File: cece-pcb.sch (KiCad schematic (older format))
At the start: 29 parts, among them J101 VAC, J102 HTU21D, J103 SERIAL, J104 Li-Ion Battery, K101 SANYOU_SRD_Form_C, Q101 Q_NPN, U101 TLV75533PDBV, U102 MCP73811T-420I-OT

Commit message: Improve ACDC converter design to make it more robust
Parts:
- removed C103: 1u, Capacitor_THT:C_Radial_D6.3mm_H5.0mm_P2.50mm, symbol Device:C
- removed J104: Li-Ion Battery, Connector_PinHeader_2.54mm:PinHeader_1x02_P2.54mm_Vertical, symbol Connector_Generic:Conn_01x02
- removed JP102: VBATT 5V, Jumper:SolderJumper-2_P1.3mm_Open_Pad1.0x1.5mm, symbol Jumper:SolderJumper_2_Open
- removed JP103: 73811, Jumper:SolderJumper-2_P1.3mm_Open_Pad1.0x1.5mm, symbol Jumper:SolderJumper_2_Open
- removed R105: R_PROG, Resistor_SMD:R_0805_2012Metric_Pad1.15x1.40mm_HandSolder, symbol Device:R_US
- removed U102: MCP73811T-420I-OT, Package_TO_SOT_SMD:SOT-23-5, symbol Battery_Management:MCP73811T-420I-OT
- added C101: 100u, Capacitor_THT:CP_Radial_D6.3mm_P2.50mm, symbol Device:CP
- added D101: SMBJ5.0A, Diode_SMD:D_SMB_Handsoldering, symbol Device:D_Zener
- added F101: 1A slow blow, Capacitor_THT:C_Disc_D8.0mm_W5.0mm_P5.00mm, symbol Device:Fuse
- added RV101: 10D561K, Capacitor_THT:C_Disc_D7.5mm_W5.0mm_P7.50mm, symbol Device:Varistor
- added VP101: VimarPlana, pol:vimar_plana_3P, symbol pol:VimarPlana
- C102: footprint Capacitor_THT:C_Radial_D6.3mm_H5.0mm_P2.50mm -> Capacitor_SMD:C_0805_2012Metric_Pad1.15x1.40mm_HandSolder
- renumbered C101 to C103, D101 to D102, D102 to D103, D103 to D105, D105 to D106, R103 to R102, R104 to R103
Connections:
- wire segments 100 -> 101
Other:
- note added: "ACDC converter schematic from:\nhttps://datasheet.lcsc.com/szlcsc/1811211452_GTL-POWER-VB02-T2S03_C335526.pdf\nWith values from:\nhttp://www.hlktech.net/product_detail.php?ProId=54"
- moved on the sheet: D104, D106, J103, PS101, U101

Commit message: Separate top and bottom PCBs
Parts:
- removed C101: 100u, Capacitor_THT:CP_Radial_D6.3mm_P2.50mm, symbol Device:CP
- removed C103: 10u, Capacitor_THT:C_Radial_D6.3mm_H5.0mm_P2.50mm, symbol Device:CP
- removed D101: SMBJ5.0A, Diode_SMD:D_SMB_Handsoldering, symbol Device:D_Zener
- removed D102: 1N4001, Diode_THT:D_DO-41_SOD81_P7.62mm_Horizontal, symbol Diode:1N4001
- removed D103, D105: LED, LED_THT:LED_D3.0mm, symbol Device:LED
- removed F101: 1A slow blow, Capacitor_THT:C_Disc_D8.0mm_W5.0mm_P5.00mm, symbol Device:Fuse
- removed H101, H102, H103, H104: MountingHole_Pad, MountingHole:MountingHole_3.2mm_M3_Pad, symbol Mechanical:MountingHole_Pad
- removed J101: VAC, TerminalBlock:TerminalBlock_bornier-5_P5.08mm, symbol Connector:Screw_Terminal_01x05
- removed JP101: VBATT_A0, Jumper:SolderJumper-2_P1.3mm_Bridged_Pad1.0x1.5mm, symbol Jumper:SolderJumper_2_Bridged
- removed K101: SANYOU_SRD_Form_C, Relay_THT:Relay_SPDT_SANYOU_SRD_Series_Form_C, symbol Relay:SANYOU_SRD_Form_C
- removed PS101: HLK-PM01, Converter_ACDC:Converter_ACDC_HiLink_HLK-PMxx, symbol Converter_ACDC:HLK-PM01
- removed Q101: Q_NPN, Package_TO_SOT_THT:TO-92L_Inline_Wide, symbol Device:Q_NPN_CBE
- removed RV101: 10D561K, Capacitor_THT:C_Disc_D7.5mm_W5.0mm_P7.50mm, symbol Device:Varistor
- added C101, C103: 1u, Capacitor_SMD:C_0805_2012Metric_Pad1.15x1.40mm_HandSolder, symbol Device:C
- added C104: 100nF, Capacitor_THT:C_Disc_D4.3mm_W1.9mm_P5.00mm, symbol Device:C
- added C105, C106: 100p, Capacitor_SMD:C_0805_2012Metric_Pad1.15x1.40mm_HandSolder, symbol Device:C
- added FB101: Ferrite_Bead, Resistor_SMD:R_0805_2012Metric_Pad1.15x1.40mm_HandSolder, symbol Device:Ferrite_Bead
- added JP101: RST, Connector_PinHeader_2.54mm:PinHeader_1x02_P2.54mm_Vertical, symbol Device:Jumper_NO_Small
- added JP102: PROG, Connector_PinHeader_2.54mm:PinHeader_1x02_P2.54mm_Vertical, symbol Device:Jumper_NO_Small
- added JP103: Deep_Sleep, Jumper:SolderJumper-2_P1.3mm_Open_Pad1.0x1.5mm, symbol Jumper:SolderJumper_2_Open
- added R104: 10k, Resistor_SMD:R_0805_2012Metric_Pad1.15x1.40mm_HandSolder, symbol Device:R_US
- added R105, R107: 330, Resistor_SMD:R_0805_2012Metric_Pad1.15x1.40mm_HandSolder, symbol Device:R_US
- added R106: 10k, Resistor_THT:R_Axial_DIN0207_L6.3mm_D2.5mm_P7.62mm_Horizontal, symbol Device:R_US
- added U102: ESP-12F/ESP07, RF_Module:ESP-07, symbol cece-pcb-rescue:ESP-12F-ESP8266-cece-pcb-rescue
- added U103: LM75C, symbol Sensor_Temperature:LM75C
- C102: value 1u -> 10u
- R101: value 220 -> 10k; footprint Resistor_THT:R_Axial_DIN0207_L6.3mm_D2.5mm_P7.62mm_Horizontal -> Resistor_SMD:R_0805_2012Metric_Pad1.15x1.40mm_HandSolder
- R102: value 1k -> 10k; footprint Resistor_THT:R_Axial_DIN0207_L6.3mm_D2.5mm_P7.62mm_Horizontal -> Resistor_SMD:R_0805_2012Metric_Pad1.15x1.40mm_HandSolder
- R103: value 100 -> 10k; footprint Resistor_THT:R_Axial_DIN0207_L6.3mm_D2.5mm_P7.62mm_Horizontal -> Resistor_SMD:R_0805_2012Metric_Pad1.15x1.40mm_HandSolder
- renumbered D104 to D101, D106 to D102, J103 to J101
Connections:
- net labels added: ADC, D0, D1|SCL, D2|SDA, D3, D4, D5|SCK, D6|MISO, D7|MOSI, D8, EN, RST
- net labels removed: +BATT, ACL, ACN, C, HTU_SCL, HTU_SDA, NC, NO, RLY
- wire segments 101 -> 99
- no-connect marks 0 -> 10
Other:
- note added: "Basic input protection from:\nhttps://www.digikey.com/en/articles/protecting-inputs-in-digital-electronics"
- note added: "https://escapequotes.net/wp-content/uploads/2016/02/wemos-d1-mini-shematics.jpg"
- note added: "https://www.wemos.cc/en/latest/_static/files/sch_d1_mini_v3.0.0.pdf"
- note removed: "ACDC converter schematic from:\nhttps://datasheet.lcsc.com/szlcsc/1811211452_GTL-POWER-VB02-T2S03_C335526.pdf\nWith values from:\nhttp://www.hlktech.net/product_detail.php?ProId=54"
- moved on the sheet: D101, D102, J101, J102

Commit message: Start defining PCB
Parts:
- added C107, C108: 100nF, Capacitor_SMD:C_0805_2012Metric_Pad1.15x1.40mm_HandSolder, symbol Device:C
- added J103: Conn_01x03_Male, Connector_PinSocket_2.54mm:PinSocket_1x03_P2.54mm_Vertical, symbol Connector:Conn_01x03_Male
- added SW101, SW102: SW_Push, Button_Switch_THT:SW_PUSH_6mm, symbol Switch:SW_Push
- C104: footprint Capacitor_THT:C_Disc_D4.3mm_W1.9mm_P5.00mm -> Capacitor_SMD:C_0805_2012Metric_Pad1.15x1.40mm_HandSolder
- R106: footprint Resistor_THT:R_Axial_DIN0207_L6.3mm_D2.5mm_P7.62mm_Horizontal -> Resistor_SMD:R_0805_2012Metric_Pad1.15x1.40mm_HandSolder
- U103: footprint (none) -> Package_SO:SOIC-8_3.9x4.9mm_P1.27mm
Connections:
- net +5V: now also J103.3 (Pin_3)
- net D4: now also SW102.1
- net D5|SCK: now also SW101.1
- net D8: now also J103.2 (Pin_2)
- net GND: now also J103.1 (Pin_1), SW101.2, SW102.2
- no-connect marks 10 -> 9
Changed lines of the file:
@@
 F 0 "U103" H 10200 6381 50  0000 C CNN
 F 1 "LM75C" H 10200 6290 50  0000 C CNN
-F 2 "" H 10200 5700 50  0001 C CNN
+F 2 "Package_SO:SOIC-8_3.9x4.9mm_P1.27mm" H 10200 5700 50  0001 C CNN
 F 3 "http://www.ti.com/lit/ds/symlink/lm75b.pdf" H 10200 5700 50  0001 C CNN
 	1    10200 5700
@@
 F 0 "C104" H 5815 3796 50  0000 L CNN
 F 1 "100nF" H 5815 3705 50  0000 L CNN
-F 2 "Capacitor_THT:C_Disc_D4.3mm_W1.9mm_P5.00mm" H 5738 3600 50  0001 C CNN
+F 2 "Capacitor_SMD:C_0805_2012Metric_Pad1.15x1.40mm_HandSolder" H 5738 3600 50  0001 C CNN
 F 3 "~" H 5700 3750 50  0001 C CNN
 	1    5700 3750
@@
 F 0 "R106" H 8232 3604 50  0000 R CNN
 F 1 "10k" H 8232 3695 50  0000 R CNN
-F 2 "Resistor_THT:R_Axial_DIN0207_L6.3mm_D2.5mm_P7.62mm_Horizontal" V 8340 3640 50  0001 C CNN
+F 2 "Resistor_SMD:R_0805_2012Metric_Pad1.15x1.40mm_HandSolder" V 8340 3640 50  0001 C CNN
 F 3 "~" H 8300 3650 50  0001 C CNN
 	1    8300 3650
@@
 	2650 5650 2650 5700
 Wire Wire Line
-	2650 5700 2500 5700
-Wire Wire Line
-	2500 5900 2650 5900
-Wire Wire Line
 	2500 6100 2650 6100
 Wire Wire Line
@@
 NoConn ~ 6150 3400
 NoConn ~ 6150 3300
-NoConn ~ 6150 3200
 NoConn ~ 6150 2900
 Text Label 8400 3300 2    50   ~ 0
@@
 Text Label 9750 5700 2    50   ~ 0
 D1|SCL
+$Comp
+L Device:C C?
+U 1 1 60A8D883
+P 10900 5650
+AR Path="/5FC173C3/60A8D883" Ref="C?"  Part="1"
+AR Path="/60A8D883" Ref="C107"  Part="1"
+F 0 "C107" H 11015 5696 50  0000 L CNN
+F 1 "100nF" H 11015 5605 50  0000 L CNN
+F 2 "Capacitor_SMD:C_0805_2012Metric_Pad1.15x1.40mm_HandSolder" H 10938 5500 50  0001 C CNN
+F 3 "~" H 10900 5650 50  0001 C CNN
+	1    10900 5650
+	1    0    0    -1
+$EndComp
+$Comp
+L Connector:Conn_01x03_Male J103
+U 1 1 60A91DC5
+P 3100 5900
+F 0 "J103" H 3072 5832 50  0000 R CNN
+F 1 "Conn_01x03_Male" H 3072 5923 50  0000 R CNN
+F 2 "Connector_PinSocket_2.54mm:PinSocket_1x03_P2.54mm_Vertical" H 3100 5900 50  0001 C CNN
+F 3 "~" H 3100 5900 50  0001 C CNN
+	1    3100 5900
+	-1   0    0    1
+$EndComp
+Wire Wire Line
+	2900 5800 2800 5800
+Wire Wire Line
+	2800 5800 2800 5700
+Wire Wire Line
+	2500 5700 2650 5700
+Connection ~ 2650 5700
+Wire Wire Line
+	2650 5700 2800 5700
+Wire Wire Line
+	2900 6000 2800 6000
+Wire Wire Line
+	2800 6000 2800 6100
+Wire Wire Line
+	2800 6100 2650 6100
+Connection ~ 2650 6100
+Wire Wire Line
+	2500 5900 2900 5900
+$Comp
+L Device:C C?
+U 1 1 60B17636
+P 7750 5700
+AR Path="/5FC173C3/60B17636" Ref="C?"  Part="1"
+AR Path="/60B17636" Ref="C108"  Part="1"
+F 0 "C108" H 7865 5746 50  0000 L CNN
+F 1 "100nF" H 7865 5655 50  0000 L CNN
+F 2 "Capacitor_SMD:C_0805_2012Metric_Pad1.15x1.40mm_HandSolder" H 7788 5550 50  0001 C CNN
+F 3 "~" H 7750 5700 50  0001 C CNN
+	1    7750 5700
+	1    0    0    -1
+$EndComp
+$Comp
+L Switch:SW_Push SW101
+U 1 1 60B1DA8F
+P 10150 3000
+F 0 "SW101" H 10150 3285 50  0000 C CNN
+F 1 "SW_Push" H 10150 3194 50  0000 C CNN
+F 2 "Button_Switch_THT:SW_PUSH_6mm" H 10150 3200 50  0001 C CNN
+F 3 "~" H 10150 3200 50  0001 C CNN
+	1    10150 3000
+	1    0    0    -1
+$EndComp
+$Comp
+L Switch:SW_Push SW102
+U 1 1 60B1ECE0
+P 10150 3500
+F 0 "SW102" H 10150 3785 50  0000 C CNN
+F 1 "SW_Push" H 10150 3694 50  0000 C CNN
+F 2 "Button_Switch_THT:SW_PUSH_6mm" H 10150 3700 50  0001 C CNN
+F 3 "~" H 10150 3700 50  0001 C CNN
+	1    10150 3500
+	1    0    0    -1
+$EndComp
+Wire Wire Line
+	10350 3000 10500 3000
+Wire Wire Line
+	10500 3000 10500 3500
+Wire Wire Line
+	10500 3500 10350 3500
+Connection ~ 10500 3500
+Wire Wire Line
+	10500 3500 10500 3700
+$Comp
+L power:GND #PWR0121
+U 1 1 60B261D7
+P 10500 3700
+F 0 "#PWR0121" H 10500 3450 50  0001 C CNN
+F 1 "GND" H 10505 3527 50  0000 C CNN
+F 2 "" H 10500 3700 50  0001 C CNN
+F 3 "" H 10500 3700 50  0001 C CNN
+	1    10500 3700
+	1    0    0    -1
+$EndComp
+Wire Wire Line
+	9950 3000 9850 3000
+Wire Wire Line
+	9950 3500 9850 3500
+Text Label 9850 3000 2    50   ~ 0
+D5|SCK
+Text Label 9850 3500 2    50   ~ 0
+D4
 $EndSCHEMATC

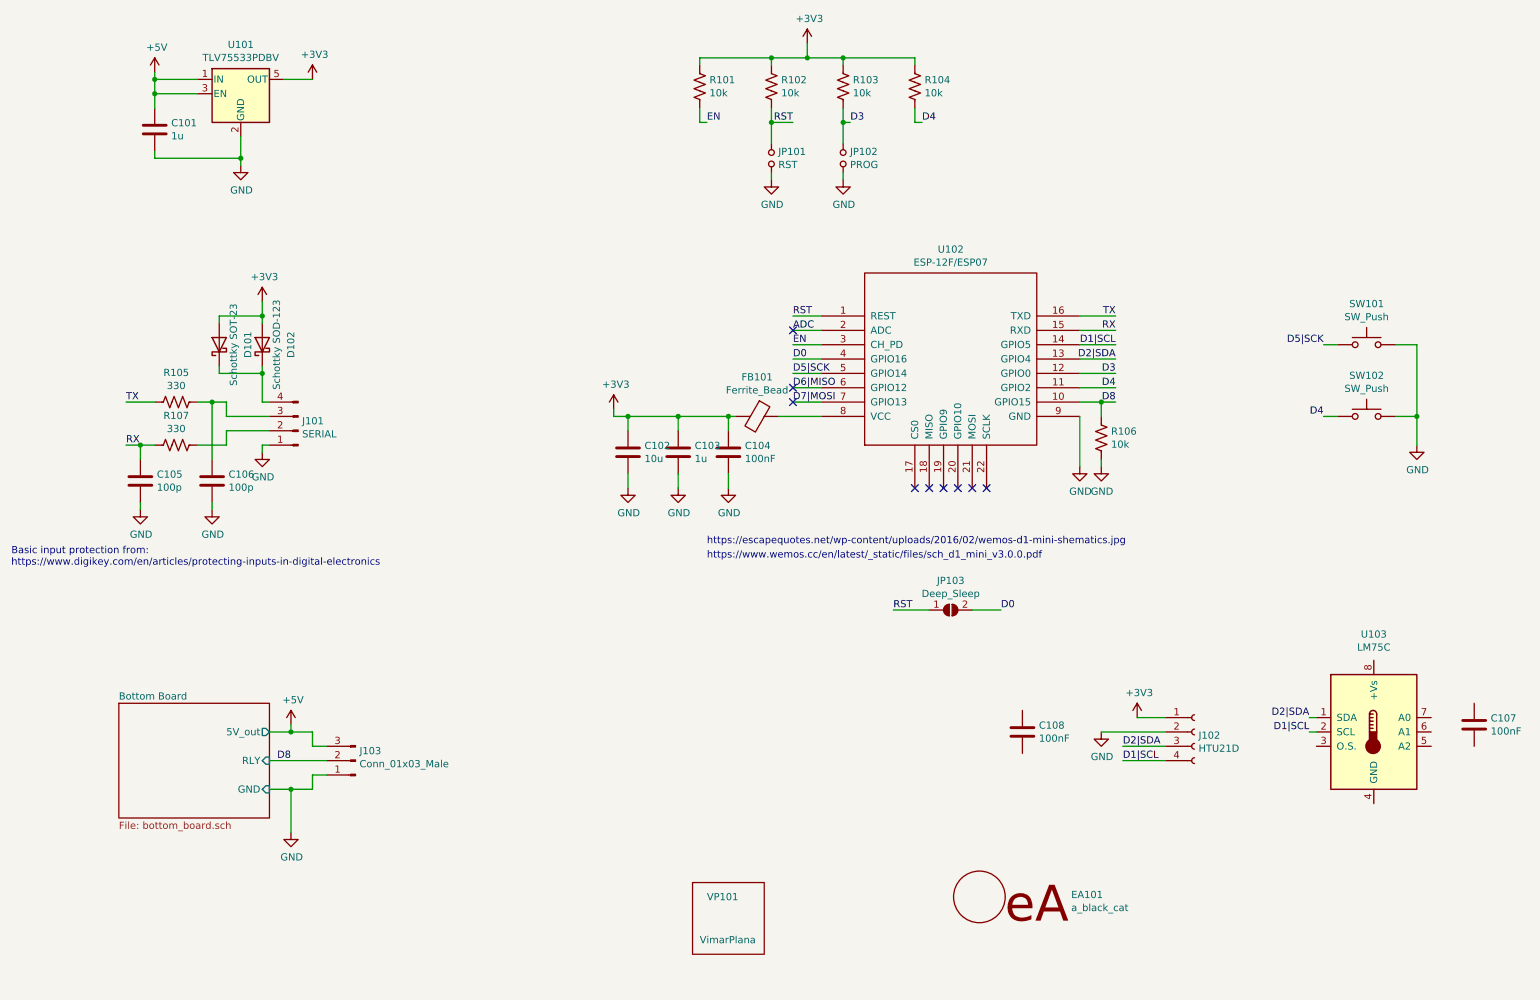
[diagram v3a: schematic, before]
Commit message: Complete the PCB ready for final review
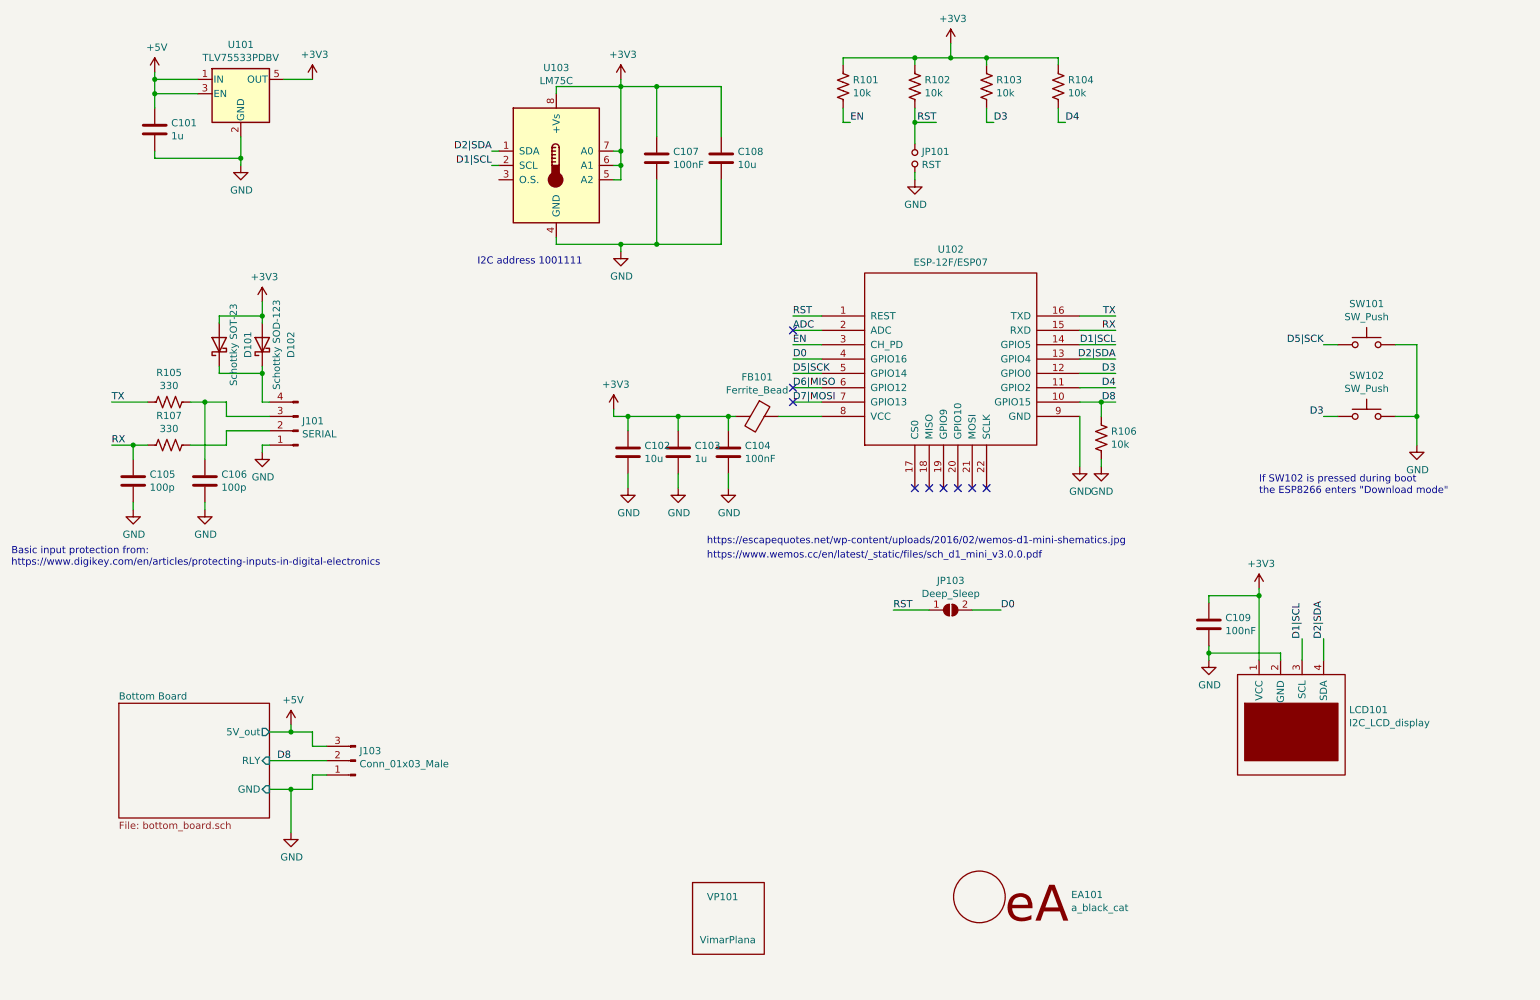
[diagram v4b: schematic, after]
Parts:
- removed J102: HTU21D, Connector_PinHeader_2.54mm:PinHeader_1x04_P2.54mm_Vertical, symbol Connector:Conn_01x04_Female
- removed JP102: PROG, Connector_PinHeader_2.54mm:PinHeader_1x02_P2.54mm_Vertical, symbol Device:Jumper_NO_Small
- added C109: 100nF, Capacitor_SMD:C_0805_2012Metric_Pad1.15x1.40mm_HandSolder, symbol Device:C
- added LCD101: I2C_LCD_display, pol:I2C_LCD_display_0.96, symbol pol:I2C_LCD_display
- C108: value 100nF -> 10u
- SW101, SW102: footprint Button_Switch_THT:SW_PUSH_6mm -> Button_Switch_SMD:SW_Push_1P1T_NO_6x6mm_H9.5mm
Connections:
- net +3V3: now also C107.1, C108.1, U103.5 (A2), U103.6 (A1), U103.7 (A0), U103.8 (+Vs), C109.1, LCD101.1 (VCC)
- net D1|SCL: now also LCD101.3 (SCL)
- net D2|SDA: now also LCD101.4 (SDA)
- net D3: now also SW102.1
- net D4: no longer SW102.1
- net GND: now also C107.2, C108.2, U103.4 (GND), C109.2, LCD101.2 (GND)
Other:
- note added: "I2C address 1001111"
- note added: "If SW102 is pressed during boot\nthe ESP8266 enters "Download mode""
- moved on the sheet: C105, C106, C107, JP101, R101, R102, R103, R104, R105, R107, U103
